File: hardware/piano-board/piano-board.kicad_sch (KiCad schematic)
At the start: 25 parts, among them J1 AVR-ISP-6, SW1 SW_SPDT, U1 ATmega328PB-A

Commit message: Design audio output on schematic
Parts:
- added C5, C6: C, symbol Device:C
- added L1: L, symbol Device:L
- added Q2: Q_PMOS_GSD, symbol Device:Q_PMOS_GSD
- added Q3: NMOS, symbol Simulation_SPICE:NMOS
- LS1: value Speaker -> PS1720P02
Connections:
- net AVCC: now also Q2.3 (D)
- net GND: now also C5.2, C6.2, Q3.1 (D)
- net MCU_AUDIO: now also Q2.1 (G), Q3.2 (G); no longer LS1.1
- new net AUDIO_AMP_OUT: C6.1, L1.1, Q2.2 (S), Q3.3 (S)
- new net AUDIO_FLTR_OUT: C5.1, L1.2, LS1.1
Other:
- note added: "Audio output"
- note added: "NOTE: Battery should be disconnected when using ISP"
- note added: "Reset"
- note added: "The audio output implements a class D amplifier"
- note removed: "Audio"
- moved on the sheet: LS1

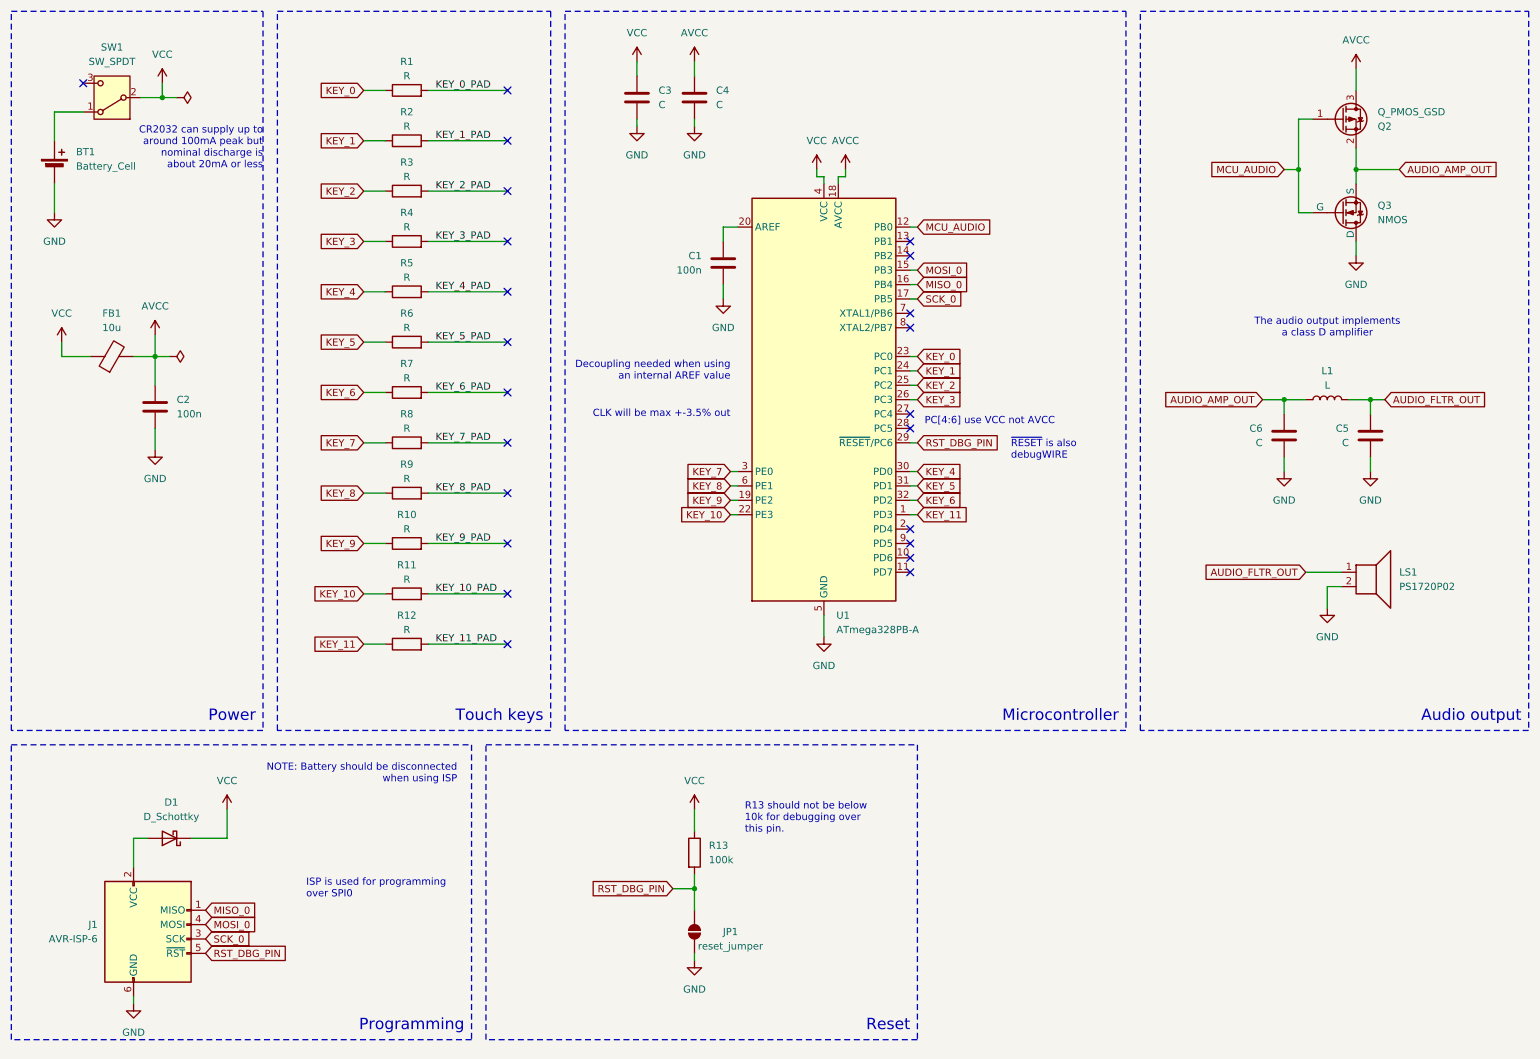
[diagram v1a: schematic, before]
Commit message: Assign footprints
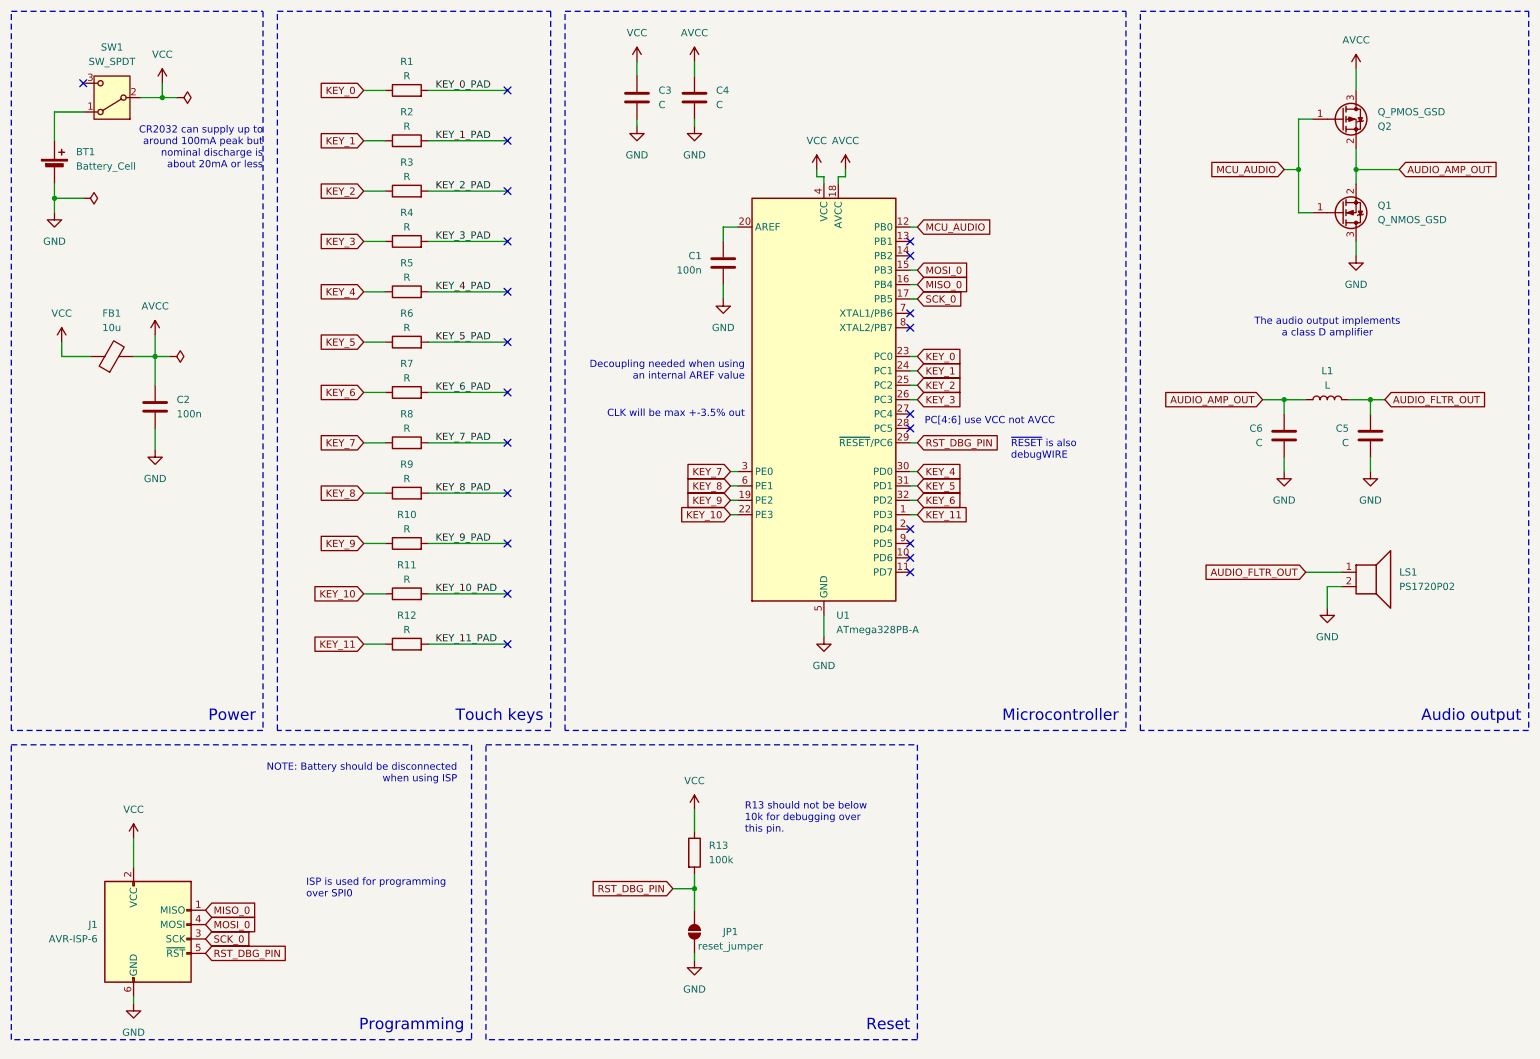
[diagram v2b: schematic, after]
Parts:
- removed D1: D_Schottky, symbol Device:D_Schottky
- removed Q3: NMOS, symbol Simulation_SPICE:NMOS
- added Q1: Q_NMOS_GSD, Package_TO_SOT_SMD:SOT-23, symbol Device:Q_NMOS_GSD
- BT1: footprint (none) -> Battery:BatteryHolder_Multicomp_BC-2001_1x2032
- C1, C2, C3, C4, C5, C6: footprint (none) -> Capacitor_SMD:C_0603_1608Metric_Pad1.08x0.95mm_HandSolder
- FB1, R1, R10, R11, R12, R13, R2, R3, R4, R5, R6, R7, R8, R9: footprint (none) -> Resistor_SMD:R_0603_1608Metric_Pad0.98x0.95mm_HandSolder
- J1: footprint (none) -> Connector_PinHeader_2.54mm:PinHeader_2x03_P2.54mm_Vertical
- LS1: footprint (none) -> Thanassis_Foot:PS1720P02
- Q2: footprint (none) -> Package_TO_SOT_SMD:SOT-23
- SW1: footprint (none) -> Thanassis_Foot:SW_SPDT_TEC_1825232-1
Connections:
- net AUDIO_AMP_OUT: now also Q1.2 (S)
- net GND: now also Q1.3 (D)
- net MCU_AUDIO: now also Q1.1 (G)
- net VCC: now also J1.2 (VCC)

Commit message: Create initial board layout
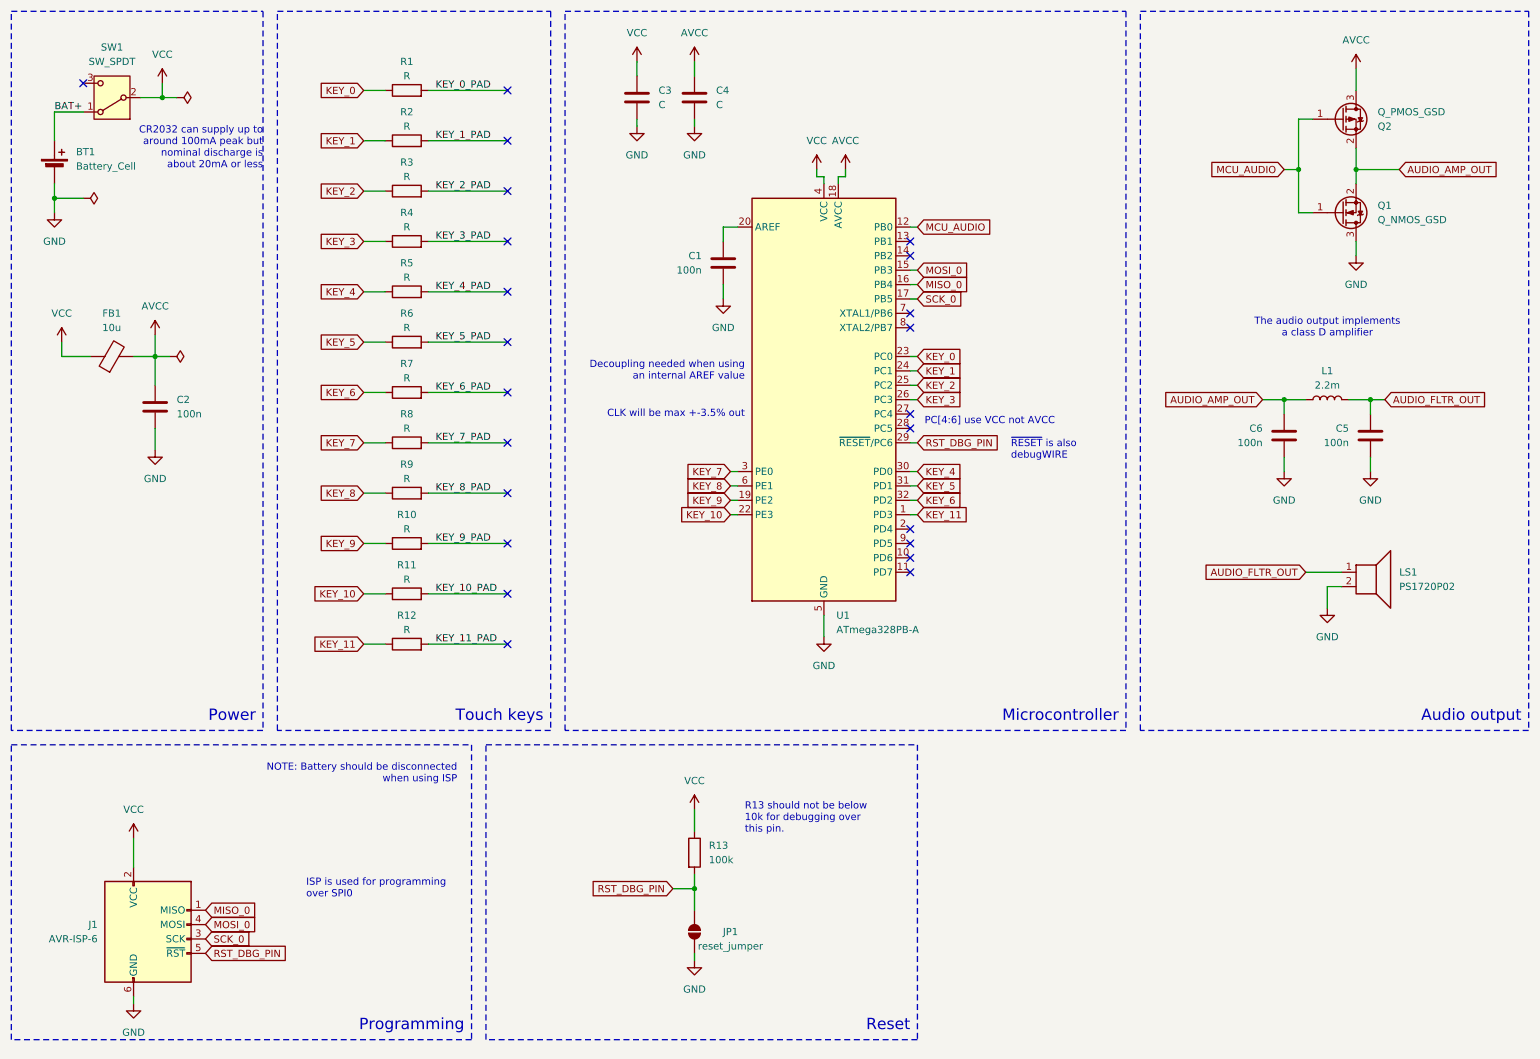
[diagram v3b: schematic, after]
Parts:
- BT1: footprint Battery:BatteryHolder_Multicomp_BC-2001_1x2032 -> Thanassis_Foot:MP000360
- C5, C6: value C -> 100n
- L1: value L -> 2.2m; footprint (none) -> Inductor_SMD:L_Coilcraft_LPS4018
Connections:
- net BAT+: now reaches BT1.1 (+), SW1.1 (A)
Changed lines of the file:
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@@
 		)
 	)
+	(label "BAT+"
+		(at 21.59 31.75 0)
+		(fields_autoplaced yes)
+		(effects
+			(font
+				(size 1.27 1.27)
+			)
+			(justify left bottom)
+		)
+	)
 	(label "KEY_7_PAD"
 		(at 88.9 90.17 0)
@@
 			)
 		)
-		(property "Footprint" "Battery:BatteryHolder_Multicomp_BC-2001_1x2032"
+		(property "Footprint" "Thanassis_Foot:MP000360"
 			(at 21.59 40.386 90)
 			(effects
@@
 			)
 		)
-		(property "Value" "C"
+		(property "Value" "100n"
 			(at 250.19 90.1699 0)
 			(effects
@@
 			)
 		)
-		(property "Value" "C"
+		(property "Value" "100n"
 			(at 234.95 90.1699 0)
 			(effects
@@
 			)
 		)
-		(property "Value" "L"
+		(property "Value" "2.2m"
 			(at 246.38 80.01 90)
 			(effects
@@
 			)
 		)
-		(property "Footprint" ""
+		(property "Footprint" "Inductor_SMD:L_Coilcraft_LPS4018"
 			(at 246.38 82.55 0)
 			(effects

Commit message: Route key connections
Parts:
- added SW2: OCT_INC, Thanassis_Foot:SW_PUSH_ADAFRUIT_SMALL, symbol Switch:SW_Push
- added SW3: OCT_DWN, Thanassis_Foot:SW_PUSH_ADAFRUIT_SMALL, symbol Switch:SW_Push
- added SW4: WAVE_CHANGE, Thanassis_Foot:SW_PUSH_ADAFRUIT_SMALL, symbol Switch:SW_Push
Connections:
- net GND: now also SW2.2, SW3.2, SW4.2
- net KEY_10: now also U1.7 (XTAL1/PB6); no longer U1.22 (PE3)
- net KEY_11: now also U1.8 (XTAL2/PB7); no longer U1.1 (PD3)
- net KEY_7: now also U1.1 (PD3); no longer U1.3 (PE0)
- net KEY_8: now also U1.2 (PD4); no longer U1.6 (PE1)
- net KEY_9: now also U1.3 (PE0); no longer U1.19 (PE2)
- net MCU_AUDIO: now also U1.22 (PE3); no longer U1.12 (PB0)
- net OCT_DEC: now reaches U1.10 (PD6)
- net OCT_DEC: now also SW3.1
- net WAVE_CHANGE: now reaches U1.11 (PD7)
- net WAVE_CHANGE: now also SW4.1
- net OCT_INC: now reaches U1.9 (PD5)
- net OCT_INC: now also SW2.1
- no-connect marks 23 -> 8
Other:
- note added: "Input"
- note added: "Reset pullup should not be below 10k for debugging over this pin."
- note removed: "R13 should not be below 10k for debugging over this pin."
- note removed: "Reset"
- moved on the sheet: JP1, R13

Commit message: Re-assign key pins on MCU
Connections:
- net KEY_10: now also U1.2 (PD4); no longer U1.7 (XTAL1/PB6)
- net KEY_11: now also U1.3 (PE0); no longer U1.8 (XTAL2/PB7)
- net KEY_4: now also U1.27 (PC4); no longer U1.30 (PD0)
- net KEY_5: now also U1.28 (PC5); no longer U1.31 (PD1)
- net KEY_6: now also U1.30 (PD0); no longer U1.32 (PD2)
- net KEY_7: now also U1.31 (PD1); no longer U1.1 (PD3)
- net KEY_8: now also U1.32 (PD2); no longer U1.2 (PD4)
- net KEY_9: now also U1.1 (PD3); no longer U1.3 (PE0)
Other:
- note added: "PC[4:6] use VCC not AVCC check if any variance is detectable"
- note removed: "PC[4:6] use VCC not AVCC"

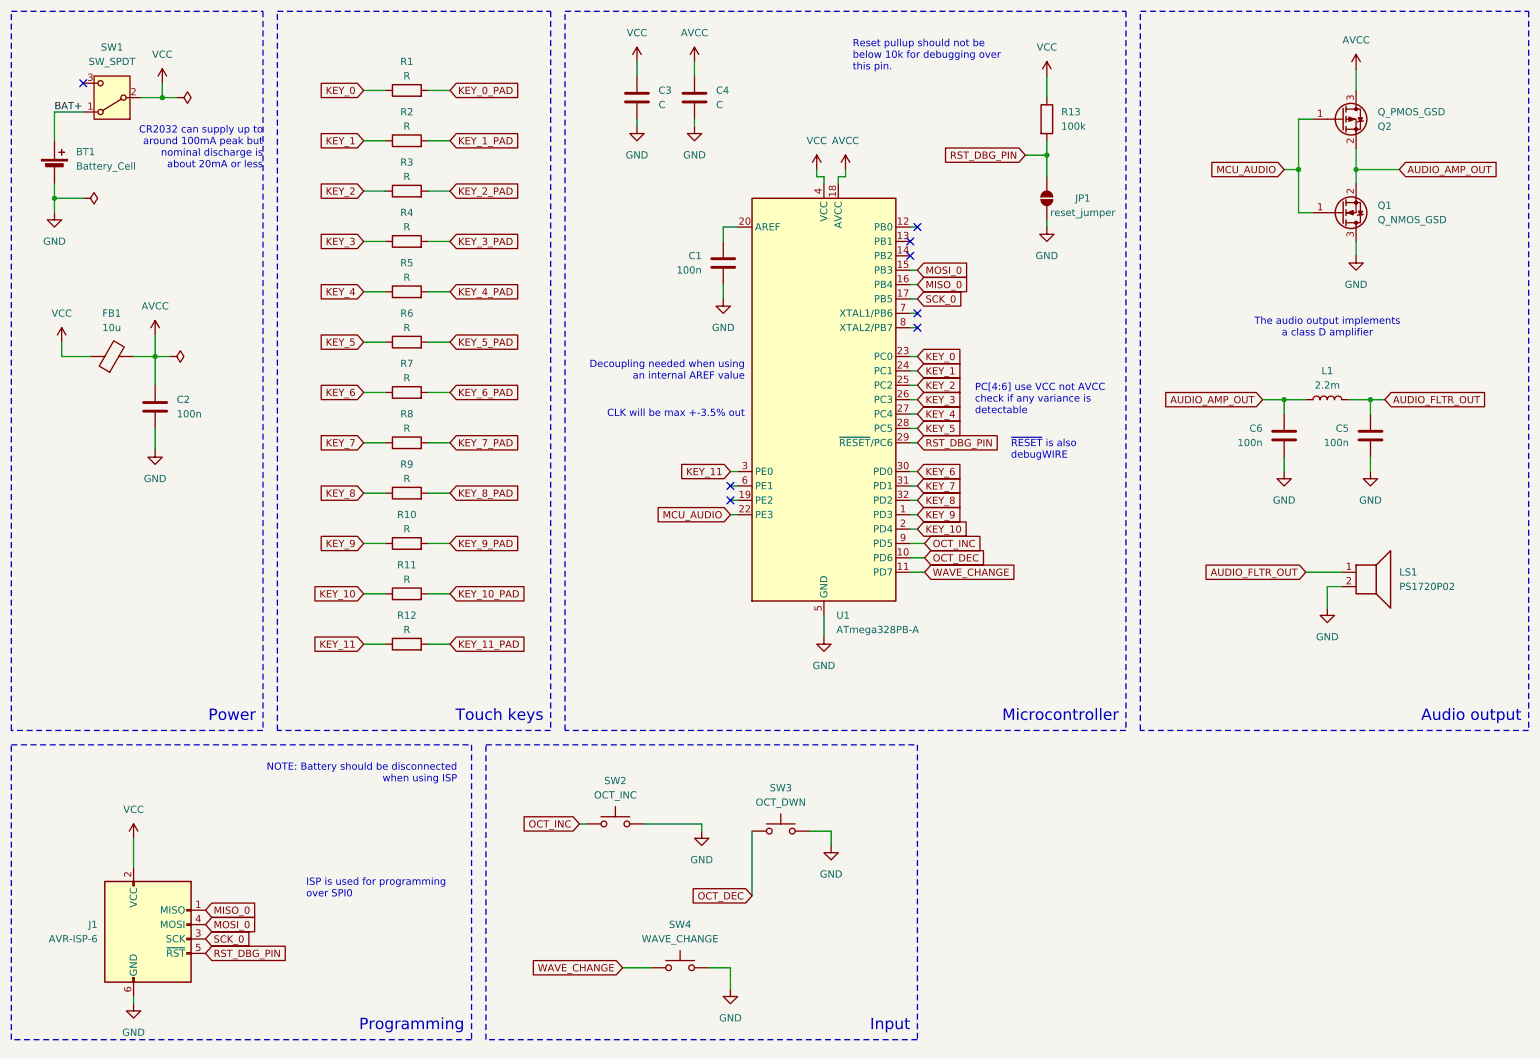
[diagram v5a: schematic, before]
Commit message: Route all signals
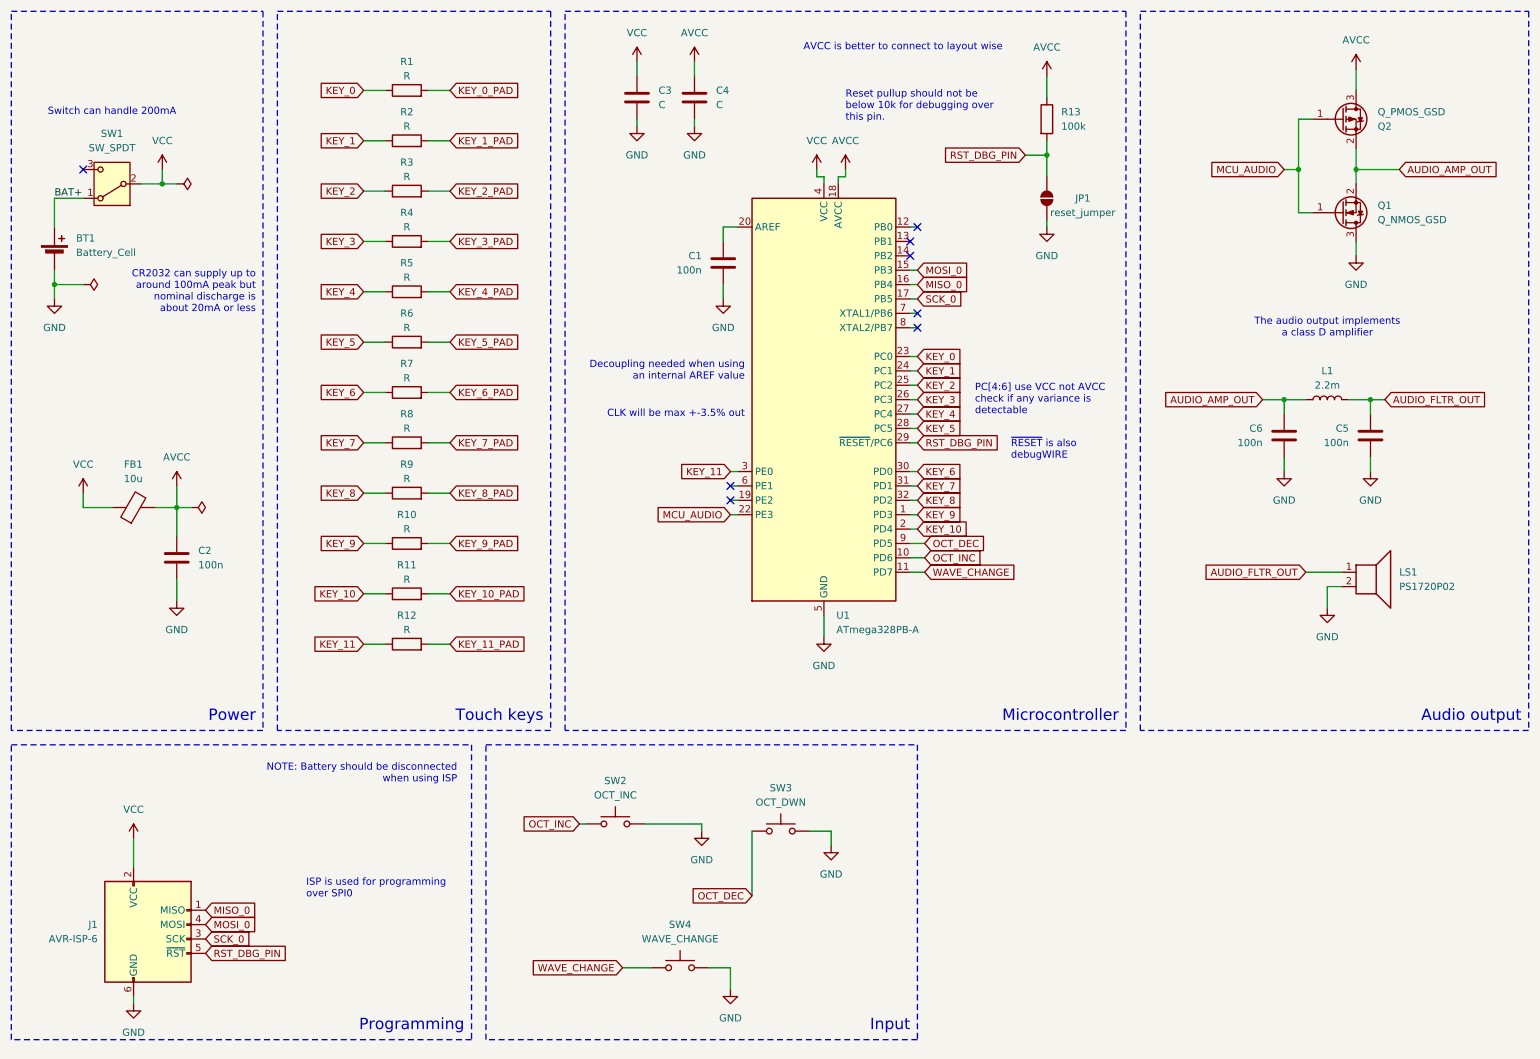
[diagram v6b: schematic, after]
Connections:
- net AVCC: now also R13.1
- net OCT_DEC: now also U1.9 (PD5); no longer U1.10 (PD6)
- net OCT_INC: now also U1.10 (PD6); no longer U1.9 (PD5)
- net VCC: no longer R13.1
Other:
- note added: "AVCC is better to connect to layout wise"
- note added: "Switch can handle 200mA"
- moved on the sheet: BT1, C2, FB1, SW1
